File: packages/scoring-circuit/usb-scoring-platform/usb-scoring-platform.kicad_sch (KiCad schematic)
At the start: 0 parts

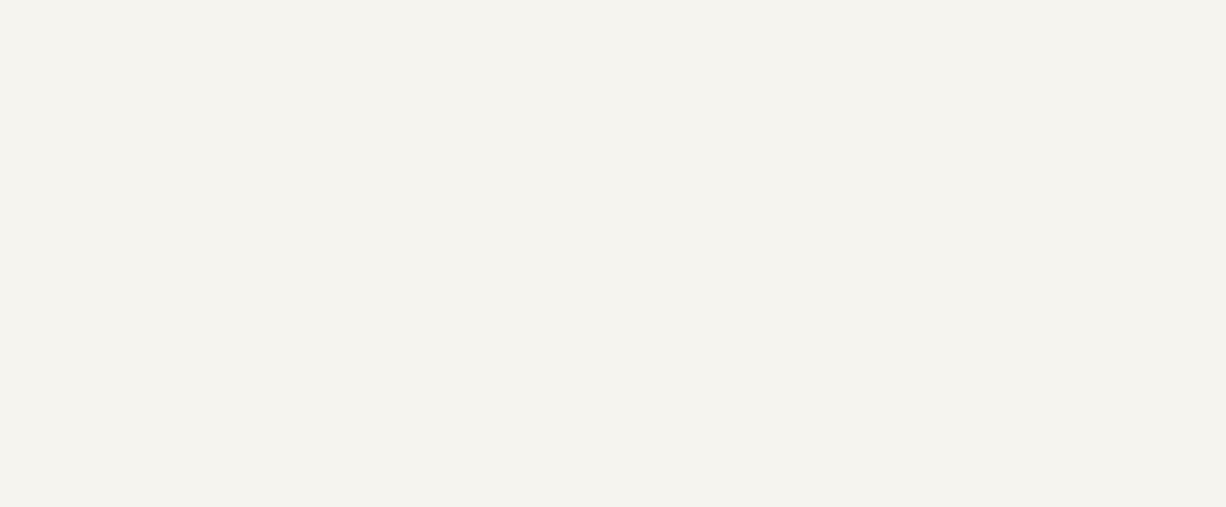
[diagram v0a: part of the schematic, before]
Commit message: feat(scoring-circuit): isolate computer USB in native KiCad draft
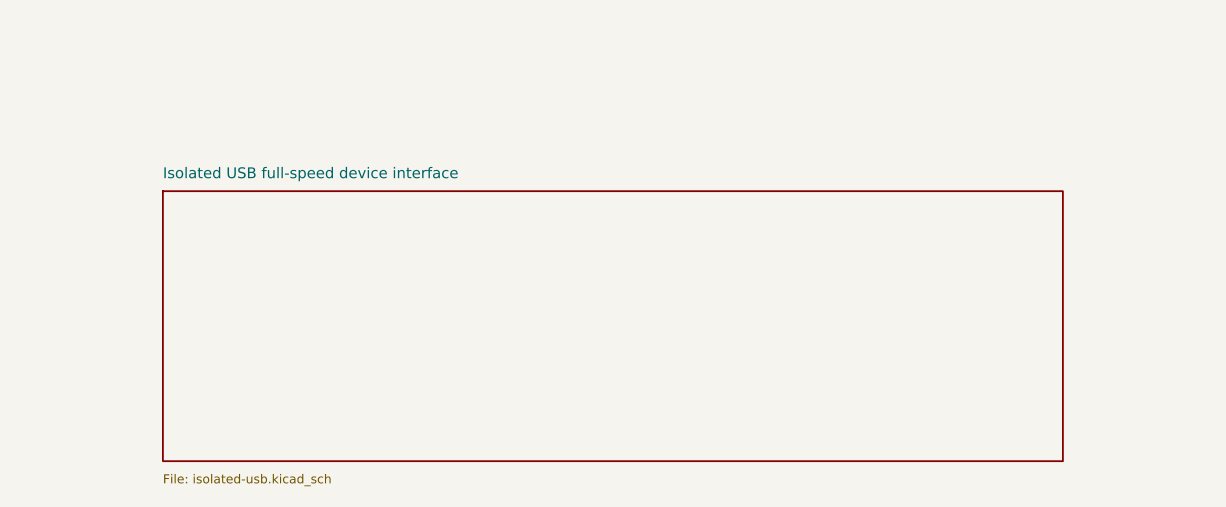
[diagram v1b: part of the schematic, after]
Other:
- added sheet Isolated USB full-speed device interface (isolated-usb.kicad_sch)

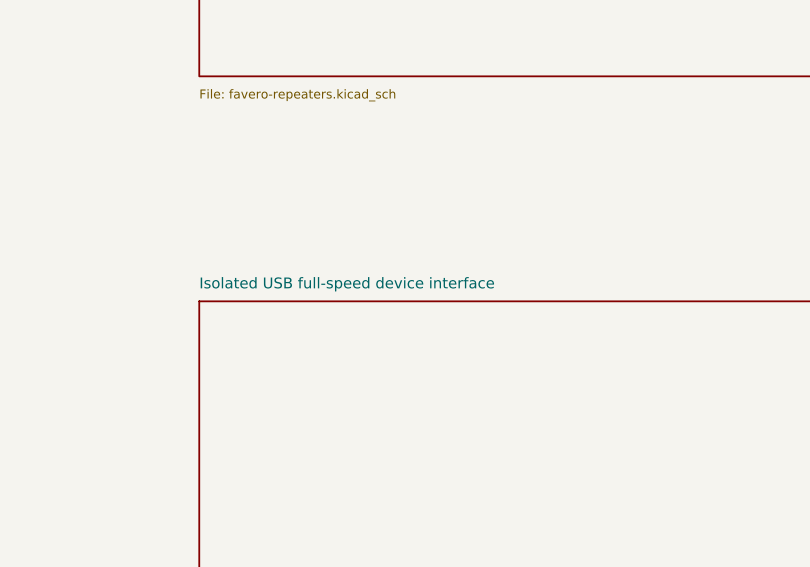
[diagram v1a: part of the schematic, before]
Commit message: feat(scoring-circuit): add isolated single-cable USB acquisition power
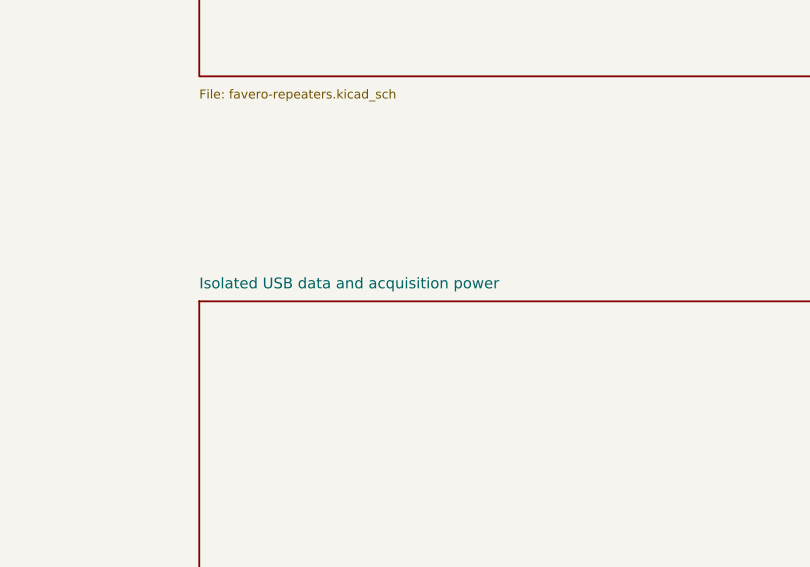
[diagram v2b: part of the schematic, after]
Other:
- sheet Isolated USB full-speed device interface renamed Isolated USB data and acquisition power

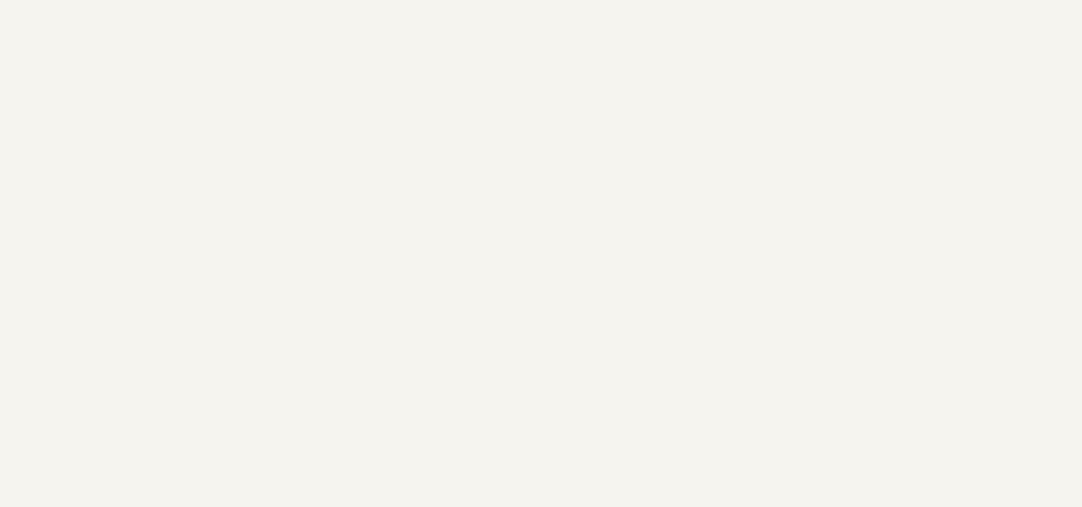
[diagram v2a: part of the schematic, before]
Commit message: feat(scoring-circuit): replace dual USB inputs with shared isolated power design
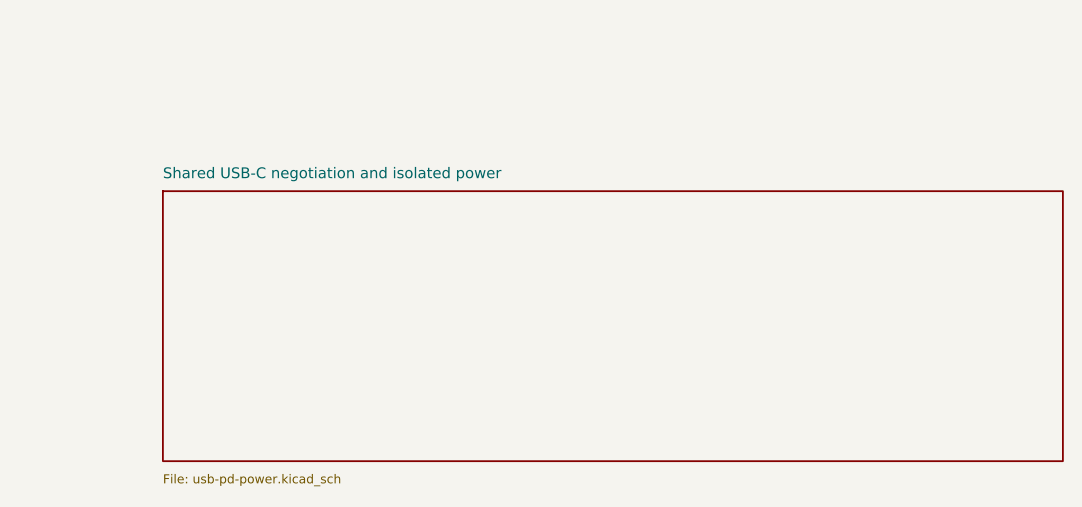
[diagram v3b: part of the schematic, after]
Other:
- added sheet Shared USB-C negotiation and isolated power (usb-pd-power.kicad_sch)
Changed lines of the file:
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@@
+(kicad_sch (version 20250114)
+(generator "eeschema")
+(paper "A3")
+(title_block (title "USB scoring platform") (rev "Engineering draft") (comment 1 "Separate design - original prototype preserved"))
+(text "USB SCORING PLATFORM - ENGINEERING DRAFT" (at 30 20 0) (effects (font (size 3 3)) (justify left)))
+(text "Desktop-first STM32 acquisition + ESP32 / Ethernet / IR / HUB75 / FA-05 / USB-C PD\nOpen each sheet to edit native symbols and nets. This design is NOT ready to fabricate or sell." (at 30 30 0) (effects (font (size 1.4 1.4)) (justify left)))
+(sheet (at 30 55) (size 100 30) (stroke (width 0.2) (type default)) (fill (color 0 0 0 0)) (property "Sheetname" "USB-C computer connection and PD power" (at 30 53 0) (effects (font (size 1.2 1.2)) (justify left))) (property "Sheetfile" "usb-and-power.kicad_sch" (at 30 87 0) (effects (font (size 1 1)) (justify left))) (instances (project "usb-scoring-platform" (path "/20cc8167-128c-446a-a106-f942323e143f" (page "2")))))
+(sheet (at 155 55) (size 100 30) (stroke (width 0.2) (type default)) (fill (color 0 0 0 0)) (property "Sheetname" "STM32 acquisition, USB and standalone scoring" (at 155 53 0) (effects (font (size 1.2 1.2)) (justify left))) (property "Sheetfile" "acquisition-controller.kicad_sch" (at 155 87 0) (effects (font (size 1 1)) (justify left))) (instances (project "usb-scoring-platform" (path "/20cc8167-128c-446a-a106-f942323e143f" (page "3")))))
+(sheet (at 280 55) (size 100 30) (stroke (width 0.2) (type default)) (fill (color 0 0 0 0)) (property "Sheetname" "Left weapon acquisition" (at 280 53 0) (effects (font (size 1.2 1.2)) (justify left))) (property "Sheetfile" "left-weapon-inputs.kicad_sch" (at 280 87 0) (effects (font (size 1 1)) (justify left))) (instances (project "usb-scoring-platform" (path "/20cc8167-128c-446a-a106-f942323e143f" (page "4")))))
+(sheet (at 30 110) (size 100 30) (stroke (width 0.2) (type default)) (fill (color 0 0 0 0)) (property "Sheetname" "Right weapon and piste acquisition" (at 30 108 0) (effects (font (size 1.2 1.2)) (justify left))) (property "Sheetfile" "right-and-piste-inputs.kicad_sch" (at 30 142 0) (effects (font (size 1 1)) (justify left))) (instances (project "usb-scoring-platform" (path "/20cc8167-128c-446a-a106-f942323e143f" (page "5")))))
+(sheet (at 155 110) (size 100 30) (stroke (width 0.2) (type default)) (fill (color 0 0 0 0)) (property "Sheetname" "ESP32 display, IR and network controller" (at 155 108 0) (effects (font (size 1.2 1.2)) (justify left))) (property "Sheetfile" "application-controller.kicad_sch" (at 155 142 0) (effects (font (size 1 1)) (justify left))) (instances (project "usb-scoring-platform" (path "/20cc8167-128c-446a-a106-f942323e143f" (page "6")))))
+(sheet (at 280 110) (size 100 30) (stroke (width 0.2) (type default)) (fill (color 0 0 0 0)) (property "Sheetname" "Populated Ethernet and IR remote" (at 280 108 0) (effects (font (size 1.2 1.2)) (justify left))) (property "Sheetfile" "ethernet-and-remote.kicad_sch" (at 280 142 0) (effects (font (size 1 1)) (justify left))) (instances (project "usb-scoring-platform" (path "/20cc8167-128c-446a-a106-f942323e143f" (page "7")))))
+(sheet (at 30 165) (size 100 30) (stroke (width 0.2) (type default)) (fill (color 0 0 0 0)) (property "Sheetname" "64x32 HUB75 and scoring sound" (at 30 163 0) (effects (font (size 1.2 1.2)) (justify left))) (property "Sheetfile" "display-and-sound.kicad_sch" (at 30 197 0) (effects (font (size 1 1)) (justify left))) (instances (project "usb-scoring-platform" (path "/20cc8167-128c-446a-a106-f942323e143f" (page "8")))))
+(sheet (at 155 165) (size 100 30) (stroke (width 0.2) (type default)) (fill (color 0 0 0 0)) (property "Sheetname" "Two FA-05 DATA-LINE repeater outputs" (at 155 163 0) (effects (font (size 1.2 1.2)) (justify left))) (property "Sheetfile" "favero-repeaters.kicad_sch" (at 155 197 0) (effects (font (size 1 1)) (justify left))) (instances (project "usb-scoring-platform" (path "/20cc8167-128c-446a-a106-f942323e143f" (page "9")))))
+(sheet (at 280 165) (size 100 30) (stroke (width 0.2) (type default)) (fill (color 0 0 0 0)) (property "Sheetname" "Defined inputs during reset and power transitions" (at 280 163 0) (effects (font (size 1.2 1.2)) (justify left))) (property "Sheetfile" "reset-defaults.kicad_sch" (at 280 197 0) (effects (font (size 1 1)) (justify left))) (instances (project "usb-scoring-platform" (path "/20cc8167-128c-446a-a106-f942323e143f" (page "10")))))
+(sheet (at 30 220) (size 100 30) (stroke (width 0.2) (type default)) (fill (color 0 0 0 0)) (property "Sheetname" "Power source declarations and design status" (at 30 218 0) (effects (font (size 1.2 1.2)) (justify left))) (property "Sheetfile" "power-declarations.kicad_sch" (at 30 252 0) (effects (font (size 1 1)) (justify left))) (instances (project "usb-scoring-platform" (path "/20cc8167-128c-446a-a106-f942323e143f" (page "11")))))
+(sheet (at 155 220) (size 100 30) (stroke (width 0.2) (type default)) (fill (color 0 0 0 0)) (property "Sheetname" "Isolated USB data and acquisition power" (at 155 218 0) (effects (font (size 1.2 1.2)) (justify left))) (property "Sheetfile" "isolated-usb.kicad_sch" (at 155 252 0) (effects (font (size 1 1)) (justify left))) (instances (project "usb-scoring-platform" (path "/20cc8167-128c-446a-a106-f942323e143f" (page "12")))))
+(sheet_instances (path "/" (page "1")))
+(embedded_fonts no)
+(sheet (at 280 220) (size 100 30) (stroke (width .2) (type default)) (fill (color 0 0 0 0)) (property "Sheetname" "Shared USB-C negotiation and isolated power" (at 280 218 0) (effects (font (size 1.2 1.2)) (justify left))) (property "Sheetfile" "usb-pd-power.kicad_sch" (at 280 252 0) (effects (font (size 1 1)) (justify left))) (instances (project "usb-scoring-platform" (path "/20cc8167-128c-446a-a106-f942323e143f" (page "13"))))))
